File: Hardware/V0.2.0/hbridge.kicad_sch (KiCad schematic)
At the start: 22 parts, among them J10 Conn_01x02, J11 Conn_01x02, J4 Conn_01x02, J5 Conn_01x02, J6 Conn_01x02, J7 Conn_01x02, J8 Conn_01x02, J9 Conn_01x02, Q2 NTMFS5H419NL, Q3 NTMFS5H419NL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

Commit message: Started first routing steps
Signed-off-by: bebenlebricolo <benoittarrade@hotmail.fr>
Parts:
- removed Q2, Q3, Q4, Q5: NTMFS5H419NL, Package_SO:ONSemi_SO-8FL_488AA, symbol Device:Q_NMOS_GDS
- added Q2, Q3, Q4, Q5: NTMFS5H419NL, BTS-MainBoard-Power:NTMFS5G419NL, symbol BTS-Power:NTMFS5H419NL
- J10, J11, J4, J5, J6, J7, J8, J9: value Conn_01x02 -> PeCon; footprint BTS-MainBoard-Power:Power_Solder_Pad_5x10mm_02 -> BTS-MainBoard-Power:TE_1-1123723-2_1x02_P3.96mm_8Amps_Vertical
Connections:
- net AHS: now also Q2.1 (S), Q2.2 (S), Q2.3 (S), Q3.5 (D)
- net BHS: now also Q4.1 (S), Q4.2 (S), Q4.3 (S), Q5.5 (D)
- net VSense: now also Q3.1 (S), Q3.2 (S), Q3.3 (S), Q5.1 (S), Q5.2 (S), Q5.3 (S)
- net Vcc: now also Q2.5 (D), Q4.5 (D)
- net BHO_Gate: now reaches R7.1
- net BHO_Gate: now also Q4.4 (G)
- net BLO_Gate: now reaches R8.1
- net BLO_Gate: now also Q5.4 (G)
- net ALO_Gate: now reaches R5.1
- net ALO_Gate: now also Q3.4 (G)
- net AHO_Gate: now reaches R4.1
- net AHO_Gate: now also Q2.4 (G)
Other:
- note added: "Peltier modules connectors array"
- moved on the sheet: C10, J10, J11, J4, J5, J6, J7, J8, J9, L1, L2, L3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

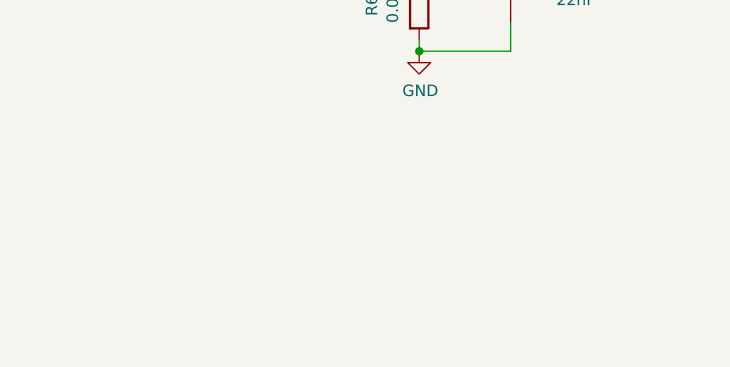
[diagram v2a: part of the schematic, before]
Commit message: Updated the board with logo and silkscreen improvements
Signed-off-by: bebenlebricolo <benoittarrade@hotmail.fr>
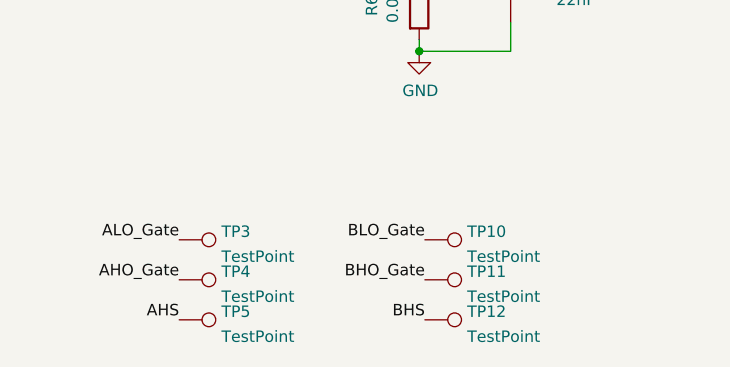
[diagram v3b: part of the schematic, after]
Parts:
- added TP10, TP11, TP12, TP3, TP4, TP5: TestPoint, TestPoint:TestPoint_Pad_D1.0mm, symbol Connector:TestPoint
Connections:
- net AHO_Gate: now also TP4.1
- net AHS: now also TP5.1
- net ALO_Gate: now also TP3.1
- net BHO_Gate: now also TP11.1
- net BHS: now also TP12.1
- net BLO_Gate: now also TP10.1
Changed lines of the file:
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@@
+    (effects (font (size 1.27 1.27)) (justify right bottom))
+  )
+  (label "AHO_Gate" (at 90.805 138.43 180)
     (effects (font (size 1.27 1.27)) (justify right bottom))
   )
@@
     (effects (font (size 1.27 1.27)) (justify right bottom))
   )
+  (label "BLO_Gate" (at 118.11 133.985 180)
+    (effects (font (size 1.27 1.27)) (justify right bottom))
+  )
   (label "+Peltier" (at 190.5 97.79 180)
     (effects (font (size 1.27 1.27)) (justify right bottom))
   )
+  (label "AHS" (at 90.805 142.875 180)
+    (effects (font (size 1.27 1.27)) (justify right bottom))
+  )
+  (label "BHO_Gate" (at 118.11 138.43 180)
+    (effects (font (size 1.27 1.27)) (justify right bottom))
+  )
   (label "-Peltier" (at 190.5 68.58 180)
     (effects (font (size 1.27 1.27)) (justify right bottom))
   )
   (label "+Peltier" (at 190.5 78.74 180)
+    (effects (font (size 1.27 1.27)) (justify right bottom))
+  )
+  (label "ALO_Gate" (at 90.805 133.985 180)
     (effects (font (size 1.27 1.27)) (justify right bottom))
   )
@@
     (effects (font (size 1.27 1.27)) (justify right bottom))
   )
+  (label "BHS" (at 118.11 142.875 180)
+    (effects (font (size 1.27 1.27)) (justify right bottom))
+  )
   (label "+Peltier" (at 190.5 91.44 180)
     (effects (font (size 1.27 1.27)) (justify right bottom))
@@
     (pin "1")
   )
+  (symbol (lib_id "Connector:TestPoint") (at 118.11 133.985 270) (unit 1)
+    (in_bom yes) (on_board yes) (fields_autoplaced)
+    (property "Reference" "TP10" (id 0) (at 122.809 133.0765 90)
+      (effects (font (size 1.27 1.27)) (justify left))
+    )
+    (property "Value" "TestPoint" (id 1) (at 122.809 135.8516 90)
+      (effects (font (size 1.27 1.27)) (justify left))
+    )
+    (property "Footprint" "TestPoint:TestPoint_Pad_D1.0mm" (id 2) (at 118.11 139.065 0)
+      (effects (font (size 1.27 1.27)) hide)
+    )
+    (property "Datasheet" "~" (id 3) (at 118.11 139.065 0)
+      (effects (font (size 1.27 1.27)) hide)
+    )
+    (pin "1")
+  )
   (symbol (lib_id "Connector_Generic:Conn_01x02") (at 195.58 53.34 0) (unit 1)
     (in_bom yes) (on_board yes)
@@
     (pin "1")
     (pin "2")
+  )
+  (symbol (lib_id "Connector:TestPoint") (at 90.805 138.43 270) (unit 1)
+    (in_bom yes) (on_board yes) (fields_autoplaced)
+    (property "Reference" "TP4" (id 0) (at 95.504 137.5215 90)
+      (effects (font (size 1.27 1.27)) (justify left))
+    )
+    (property "Value" "TestPoint" (id 1) (at 95.504 140.2966 90)
+      (effects (font (size 1.27 1.27)) (justify left))
+    )
+    (property "Footprint" "TestPoint:TestPoint_Pad_D1.0mm" (id 2) (at 90.805 143.51 0)
+      (effects (font (size 1.27 1.27)) hide)
+    )
+    (property "Datasheet" "~" (id 3) (at 90.805 143.51 0)
+      (effects (font (size 1.27 1.27)) hide)
+    )
+    (pin "1")
   )
   (symbol (lib_id "Connector_Generic:Conn_01x02") (at 195.58 72.39 0) (unit 1)
@@
     (pin "5")
   )
+  (symbol (lib_id "Connector:TestPoint") (at 118.11 142.875 270) (unit 1)
+    (in_bom yes) (on_board yes) (fields_autoplaced)
+    (property "Reference" "TP12" (id 0) (at 122.809 141.9665 90)
+      (effects (font (size 1.27 1.27)) (justify left))
+    )
+    (property "Value" "TestPoint" (id 1) (at 122.809 144.7416 90)
+      (effects (font (size 1.27 1.27)) (justify left))
+    )
+    (property "Footprint" "TestPoint:TestPoint_Pad_D1.0mm" (id 2) (at 118.11 147.955 0)
+      (effects (font (size 1.27 1.27)) hide)
+    )
+    (property "Datasheet" "~" (id 3) (at 118.11 147.955 0)
+      (effects (font (size 1.27 1.27)) hide)
+    )
+    (pin "1")
+  )
   (symbol (lib_id "Device:L") (at 107.95 76.835 90) (unit 1)
     (in_bom yes) (on_board yes)
@@
     (pin "2")
   )
+  (symbol (lib_id "Connector:TestPoint") (at 90.805 142.875 270) (unit 1)
+    (in_bom yes) (on_board yes) (fields_autoplaced)
+    (property "Reference" "TP5" (id 0) (at 95.504 141.9665 90)
+      (effects (font (size 1.27 1.27)) (justify left))
+    )
+    (property "Value" "TestPoint" (id 1) (at 95.504 144.7416 90)
+      (effects (font (size 1.27 1.27)) (justify left))
+    )
+    (property "Footprint" "TestPoint:TestPoint_Pad_D1.0mm" (id 2) (at 90.805 147.955 0)
+      (effects (font (size 1.27 1.27)) hide)
+    )
+    (property "Datasheet" "~" (id 3) (at 90.805 147.955 0)
+      (effects (font (size 1.27 1.27)) hide)
+    )
+    (pin "1")
+  )
   (symbol (lib_id "Connector_Generic:Conn_01x02") (at 195.58 97.79 0) (unit 1)
     (in_bom yes) (on_board yes)
@@
     (pin "5")
   )
+  (symbol (lib_id "Connector:TestPoint") (at 118.11 138.43 270) (unit 1)
+    (in_bom yes) (on_board yes) (fields_autoplaced)
+    (property "Reference" "TP11" (id 0) (at 122.809 137.5215 90)
+      (effects (font (size 1.27 1.27)) (justify left))
+    )
+    (property "Value" "TestPoint" (id 1) (at 122.809 140.2966 90)
+      (effects (font (size 1.27 1.27)) (justify left))
+    )
+    (property "Footprint" "TestPoint:TestPoint_Pad_D1.0mm" (id 2) (at 118.11 143.51 0)
+      (effects (font (size 1.27 1.27)) hide)
+    )
+    (property "Datasheet" "~" (id 3) (at 118.11 143.51 0)
+      (effects (font (size 1.27 1.27)) hide)
+    )
+    (pin "1")
+  )
   (symbol (lib_id "Device:L") (at 107.95 73.66 90) (unit 1)
     (in_bom yes) (on_board yes)
@@
     (pin "2")
   )
+  (symbol (lib_id "Connector:TestPoint") (at 90.805 133.985 270) (unit 1)
+    (in_bom yes) (on_board yes) (fields_autoplaced)
+    (property "Reference" "TP3" (id 0) (at 95.504 133.0765 90)
+      (effects (font (size 1.27 1.27)) (justify left))
+    )
+    (property "Value" "TestPoint" (id 1) (at 95.504 135.8516 90)
+      (effects (font (size 1.27 1.27)) (justify left))
+    )
+    (property "Footprint" "TestPoint:TestPoint_Pad_D1.0mm" (id 2) (at 90.805 139.065 0)
+      (effects (font (size 1.27 1.27)) hide)
+    )
+    (property "Datasheet" "~" (id 3) (at 90.805 139.065 0)
+      (effects (font (size 1.27 1.27)) hide)
+    )
+    (pin "1")
+  )
   (symbol (lib_id "Device:R") (at 87.63 53.975 270) (unit 1)
